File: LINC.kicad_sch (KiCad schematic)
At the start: 0 parts

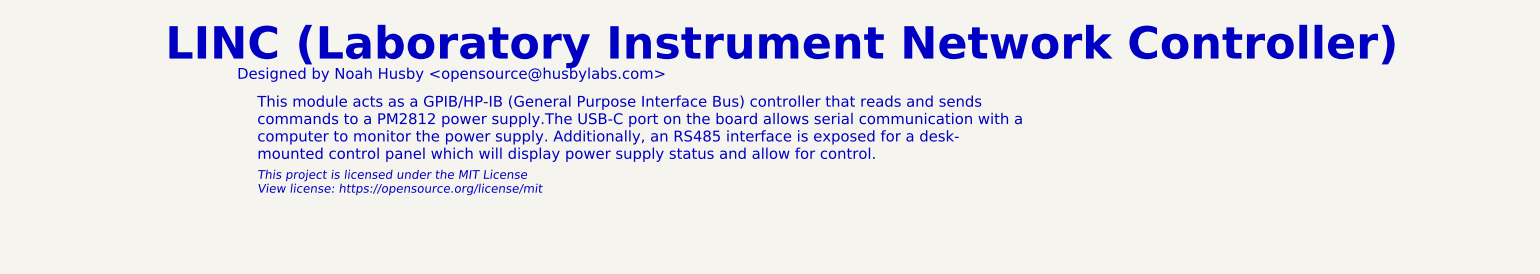
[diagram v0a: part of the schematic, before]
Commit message: Update graphics and license
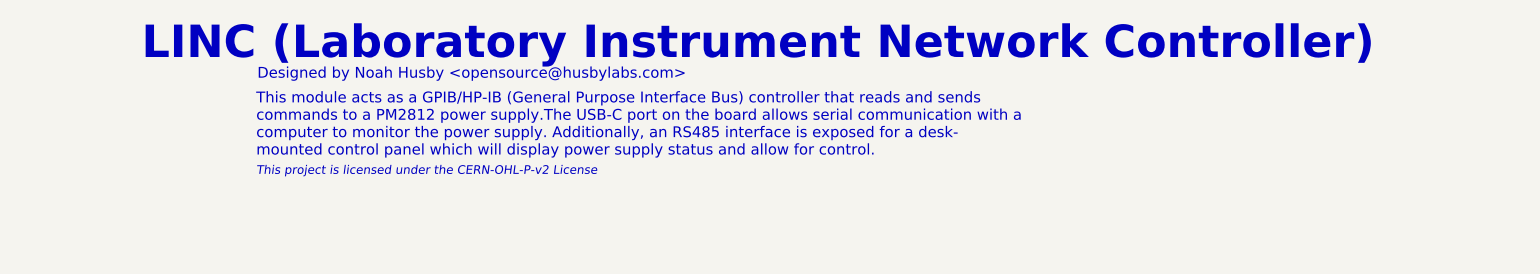
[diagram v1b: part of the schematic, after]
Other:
- note added: "This project is licensed under the CERN-OHL-P-v2 License"
- note removed: "This project is licensed under the MIT License View license: https://opensource.org/license/mit"
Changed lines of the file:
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@@
 		(rev "0.1")
 	)
-	(text "This project is licensed under the MIT License\nView license: https://opensource.org/license/mit"
+	(text "This project is licensed under the CERN-OHL-P-v2 License"
 		(exclude_from_sim no)
-		(at 25.4 66.04 0)
+		(at 25.146 63.246 0)
 		(effects
 			(font
-				(face "Helvetica")
+				(face "Times New Roman")
 				(size 2.032 2.032)
 				(italic yes)
@@
 	(text "Designed by Noah Husby <opensource@husbylabs.com>"
 		(exclude_from_sim no)
-		(at 71.12 40.64 0)
+		(at 25.4 40.386 0)
 		(effects
 			(font
-				(face "Helvetica")
+				(face "Times New Roman")
 				(size 2.54 2.54)
 				(color 0 0 0 1)
 			)
+			(justify left)
 		)
 	)
 	(text "This module acts as a GPIB/HP-IB (General Purpose Interface Bus) controller that reads and sends \ncommands to a PM2812 power supply.The USB-C port on the board allows serial communication with a \ncomputer to monitor the power supply. Additionally, an RS485 interface is exposed for a desk-\nmounted control panel which will display power supply status and allow for control."
 		(exclude_from_sim no)
-		(at 25.4 53.34 0)
+		(at 25.146 52.324 0)
 		(effects
 			(font
-				(face "Helvetica")
+				(face "Times New Roman")
 				(size 2.54 2.54)
 				(color 0 0 0 1)
@@
 	(text "LINC (Laboratory Instrument Network Controller)"
 		(exclude_from_sim no)
-		(at 148.844 33.528 0)
+		(at 143.256 28.702 0)
 		(effects
 			(font
-				(face "Helvetica")
+				(face "Times New Roman")
 				(size 7.62 7.62)
 				(bold yes)
 				(color 0 0 0 1)
 			)
+			(justify top)
 		)
 	)
